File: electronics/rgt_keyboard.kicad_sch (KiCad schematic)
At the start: 30 parts, among them SW30 SW_SPST, SW31 SW_SPST, SW32 SW_SPST, SW33 SW_SPST, SW34 SW_SPST, SW35 SW_SPST, SW36 SW_SPST, SW37 SW_SPST, SW38 SW_SPST, SW39 SW_SPST, SW40 SW_SPST, SW41 SW_SPST, SW42 SW_SPST, SW43 SW_SPST, SW44 SW_SPST, SW45 SW_SPST, SW46 SW_SPST, SW47 SW_SPST, SW48 SW_SPST, SW49 SW_SPST, SW50 SW_SPST, SW51 SW_SPST, SW52 SW_SPST, SW53 SW_SPST, SW54 SW_SPST, SW55 SW_SPST, SW56 SW_SPST, SW57 SW_SPST, SW58 SW_SPST, U3 PCA9506DGG

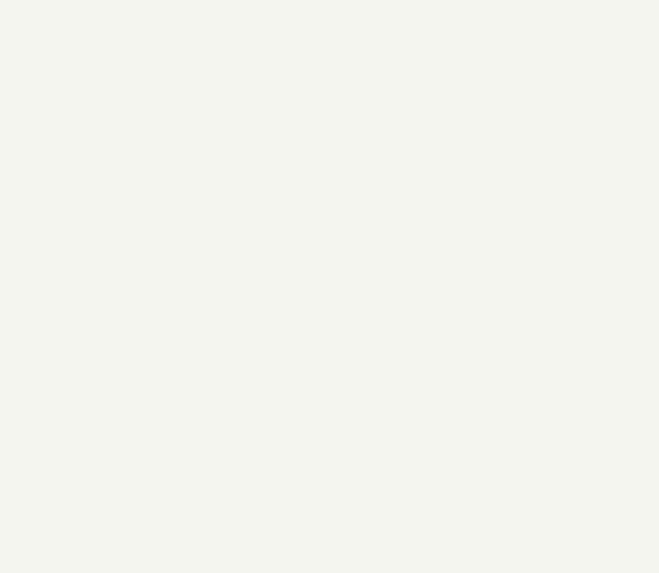
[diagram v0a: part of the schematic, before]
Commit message: add i2c headers to schematic
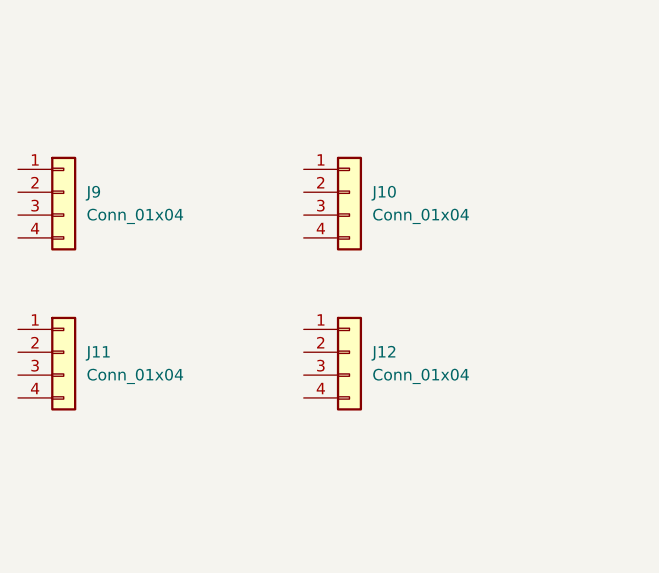
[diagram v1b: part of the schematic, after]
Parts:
- added J10, J11, J12, J9: Conn_01x04, symbol Connector_Generic:Conn_01x04
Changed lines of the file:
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@@
     (pin "2")
+  )
+  (symbol (lib_id "Connector_Generic:Conn_01x04") (at 43.18 66.04 0) (unit 1)
+    (in_bom yes) (on_board yes) (fields_autoplaced)
+    (property "Reference" "J11" (id 0) (at 45.72 66.0399 0)
+      (effects (font (size 1.27 1.27)) (justify left))
+    )
+    (property "Value" "Conn_01x04" (id 1) (at 45.72 68.5799 0)
+      (effects (font (size 1.27 1.27)) (justify left))
+    )
+    (property "Footprint" "" (id 2) (at 43.18 66.04 0)
+      (effects (font (size 1.27 1.27)) hide)
+    )
+    (property "Datasheet" "~" (id 3) (at 43.18 66.04 0)
+      (effects (font (size 1.27 1.27)) hide)
+    )
+    (pin "1")
+    (pin "2")
+    (pin "3")
+    (pin "4")
   )
   (symbol (lib_name "SW_SPST_2") (lib_id "Kailh:SW_SPST") (at 44.45 133.35 0) (unit 1)
@@
     (pin "2")
   )
+  (symbol (lib_id "Connector_Generic:Conn_01x04") (at 43.18 48.26 0) (unit 1)
+    (in_bom yes) (on_board yes) (fields_autoplaced)
+    (property "Reference" "J9" (id 0) (at 45.72 48.2599 0)
+      (effects (font (size 1.27 1.27)) (justify left))
+    )
+    (property "Value" "Conn_01x04" (id 1) (at 45.72 50.7999 0)
+      (effects (font (size 1.27 1.27)) (justify left))
+    )
+    (property "Footprint" "" (id 2) (at 43.18 48.26 0)
+      (effects (font (size 1.27 1.27)) hide)
+    )
+    (property "Datasheet" "~" (id 3) (at 43.18 48.26 0)
+      (effects (font (size 1.27 1.27)) hide)
+    )
+    (pin "1")
+    (pin "2")
+    (pin "3")
+    (pin "4")
+  )
   (symbol (lib_name "SW_SPST_26") (lib_id "Kailh:SW_SPST") (at 44.45 101.6 0) (unit 1)
     (in_bom yes) (on_board yes) (fields_autoplaced)
@@
     (pin "2")
   )
+  (symbol (lib_id "Connector_Generic:Conn_01x04") (at 74.93 66.04 0) (unit 1)
+    (in_bom yes) (on_board yes) (fields_autoplaced)
+    (property "Reference" "J12" (id 0) (at 77.47 66.0399 0)
+      (effects (font (size 1.27 1.27)) (justify left))
+    )
+    (property "Value" "Conn_01x04" (id 1) (at 77.47 68.5799 0)
+      (effects (font (size 1.27 1.27)) (justify left))
+    )
+    (property "Footprint" "" (id 2) (at 74.93 66.04 0)
+      (effects (font (size 1.27 1.27)) hide)
+    )
+    (property "Datasheet" "~" (id 3) (at 74.93 66.04 0)
+      (effects (font (size 1.27 1.27)) hide)
+    )
+    (pin "1")
+    (pin "2")
+    (pin "3")
+    (pin "4")
+  )
+  (symbol (lib_id "Connector_Generic:Conn_01x04") (at 74.93 48.26 0) (unit 1)
+    (in_bom yes) (on_board yes) (fields_autoplaced)
+    (property "Reference" "J10" (id 0) (at 77.47 48.2599 0)
+      (effects (font (size 1.27 1.27)) (justify left))
+    )
+    (property "Value" "Conn_01x04" (id 1) (at 77.47 50.7999 0)
+      (effects (font (size 1.27 1.27)) (justify left))
+    )
+    (property "Footprint" "" (id 2) (at 74.93 48.26 0)
+      (effects (font (size 1.27 1.27)) hide)
+    )
+    (property "Datasheet" "~" (id 3) (at 74.93 48.26 0)
+      (effects (font (size 1.27 1.27)) hide)
+    )
+    (pin "1")
+    (pin "2")
+    (pin "3")
+    (pin "4")
+  )
   (symbol (lib_name "SW_SPST_4") (lib_id "Kailh:SW_SPST") (at 64.77 149.86 0) (unit 1)

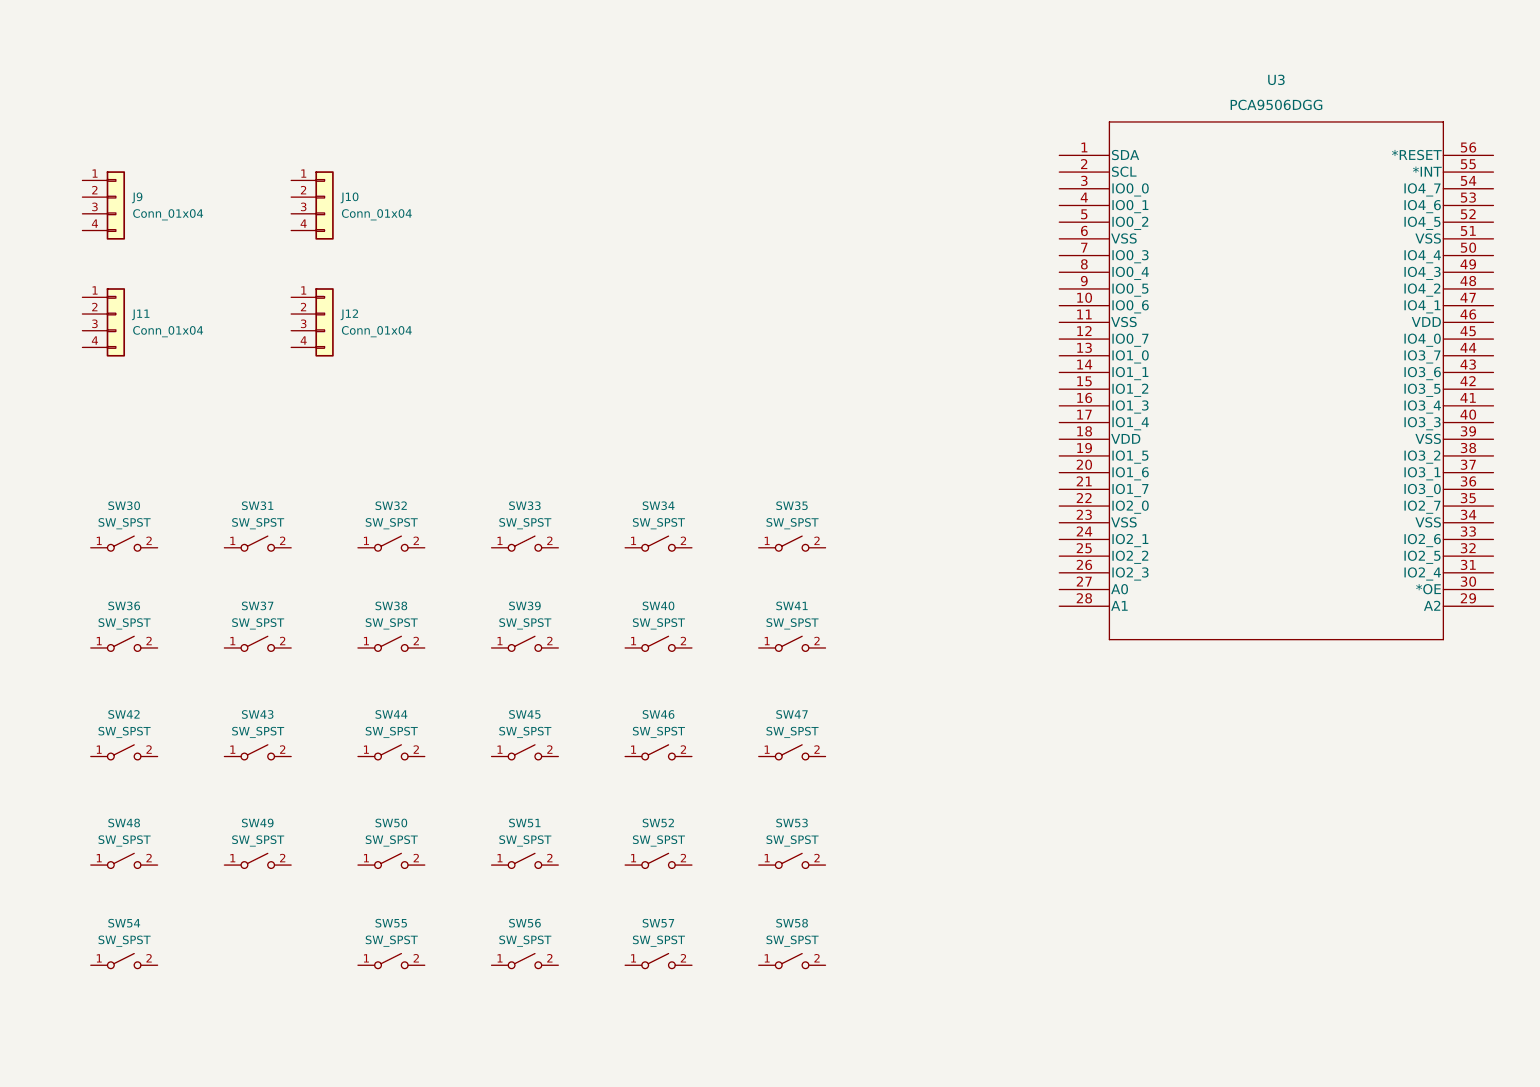
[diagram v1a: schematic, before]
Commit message: label switch nets
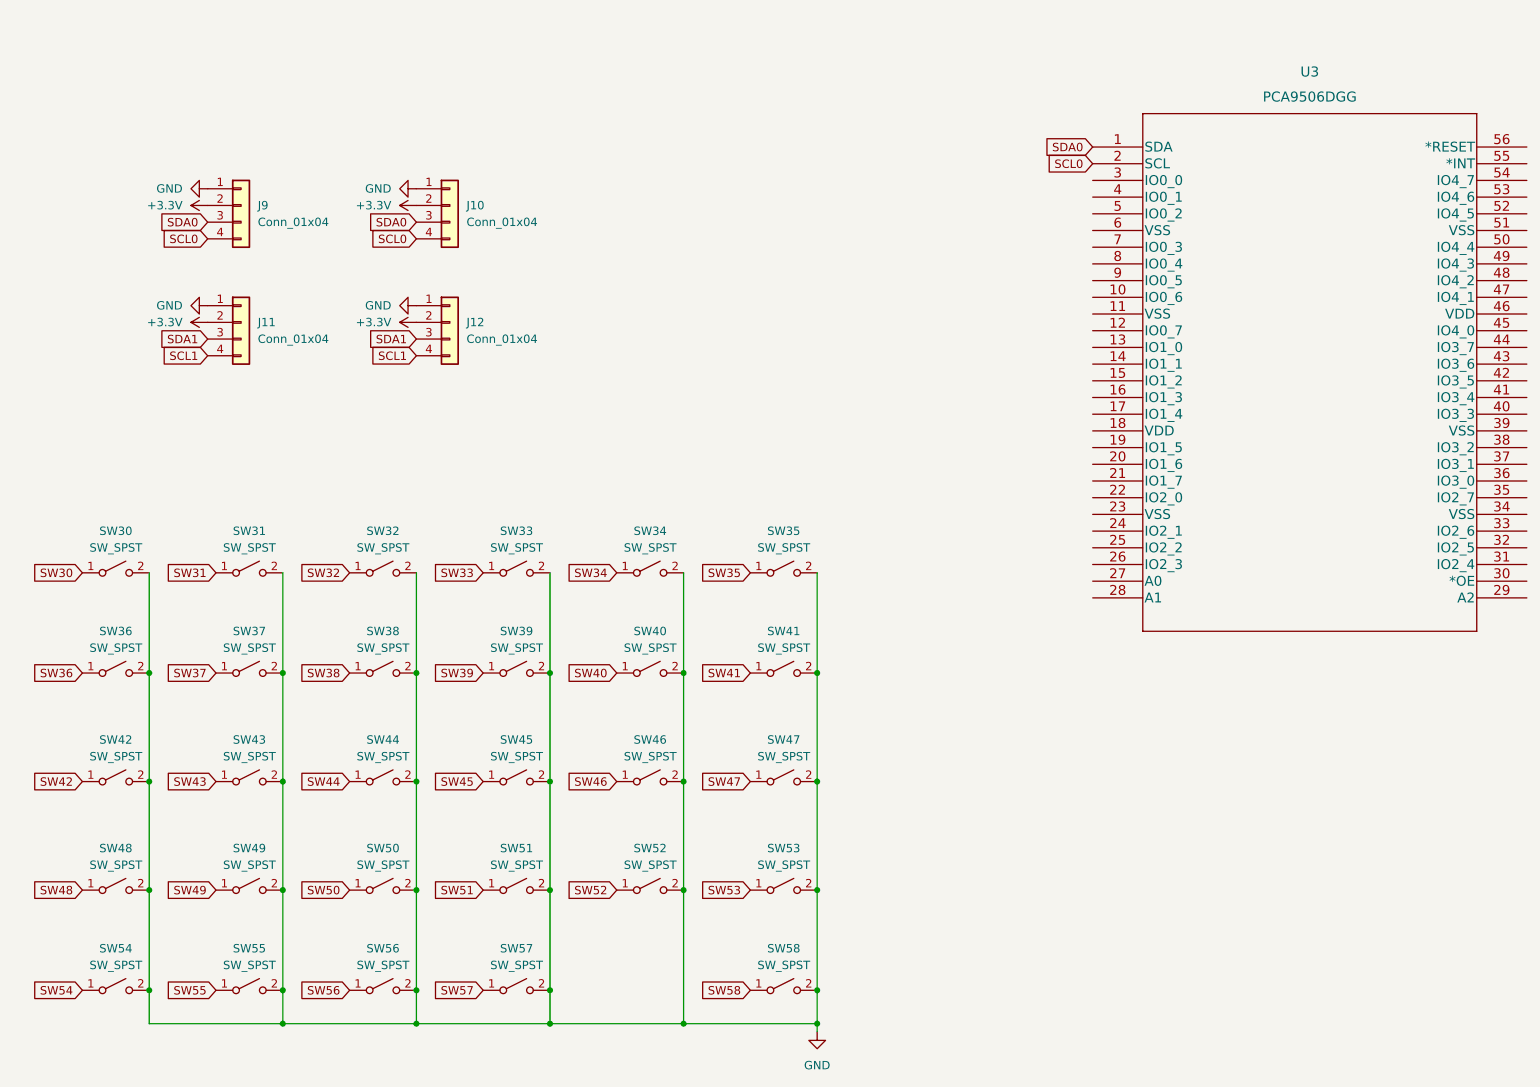
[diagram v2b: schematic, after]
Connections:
- net SW31: now reaches SW31.1 (A)
- net GND: now reaches SW31.2 (B)
- net GND: now also J10.1 (Pin_1), J11.1 (Pin_1), J12.1 (Pin_1), J9.1 (Pin_1), SW30.2 (B), SW32.2 (B), SW33.2 (B), SW34.2 (B), SW35.2 (B), SW36.2 (B), SW37.2 (B), SW38.2 (B), SW39.2 (B), SW40.2 (B), SW41.2 (B), SW42.2 (B), SW43.2 (B), SW44.2 (B), SW45.2 (B), SW46.2 (B), SW47.2 (B), SW48.2 (B), SW49.2 (B), SW50.2 (B), SW51.2 (B), SW52.2 (B), SW53.2 (B), SW54.2 (B), SW55.2 (B), SW56.2 (B), SW57.2 (B), SW58.2 (B)
- net SW44: now reaches SW44.1 (A)
- net SW39: now reaches SW39.1 (A)
- net +3V3: now reaches J11.2 (Pin_2)
- net +3V3: now also J10.2 (Pin_2), J12.2 (Pin_2), J9.2 (Pin_2)
- net SDA1: now reaches J11.3 (Pin_3)
- net SDA1: now also J12.3 (Pin_3)
- net SCL1: now reaches J11.4 (Pin_4)
- net SCL1: now also J12.4 (Pin_4)
- net SW42: now reaches SW42.1 (A)
- net SW55: now reaches SW55.1 (A)
- net SDA0: now reaches J9.3 (Pin_3)
- net SDA0: now also J10.3 (Pin_3), U3.1 (SDA)
- net SCL0: now reaches J9.4 (Pin_4)
- net SCL0: now also J10.4 (Pin_4), U3.2 (SCL)
- net SW30: now reaches SW30.1 (A)
- net SW37: now reaches SW37.1 (A)
- net SW49: now reaches SW49.1 (A)
- net SW46: now reaches SW46.1 (A)
- net SW50: now reaches SW50.1 (A)
- net SW40: now reaches SW40.1 (A)
- net SW32: now reaches SW32.1 (A)
- net SW45: now reaches SW45.1 (A)
- net SW52: now reaches SW52.1 (A)
- net SW33: now reaches SW33.1 (A)
- net SW35: now reaches SW35.1 (A)
- net SW36: now reaches SW36.1 (A)
- net SW34: now reaches SW34.1 (A)
- net SW54: now reaches SW54.1 (A)
- net SW57: now reaches SW57.1 (A)
- net SW53: now reaches SW53.1 (A)
- net SW41: now reaches SW41.1 (A)
- net SW38: now reaches SW38.1 (A)
- net SW48: now reaches SW48.1 (A)
- net SW51: now reaches SW51.1 (A)
- net SW43: now reaches SW43.1 (A)
- net SW47: now reaches SW47.1 (A)
- net SW56: now reaches SW56.1 (A)
- net SW58: now reaches SW58.1 (A)

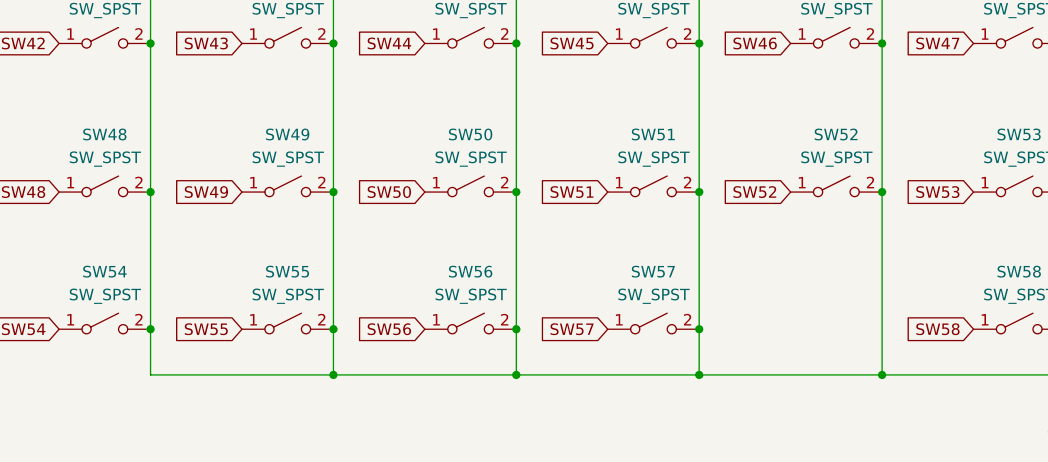
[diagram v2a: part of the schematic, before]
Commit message: move some switches
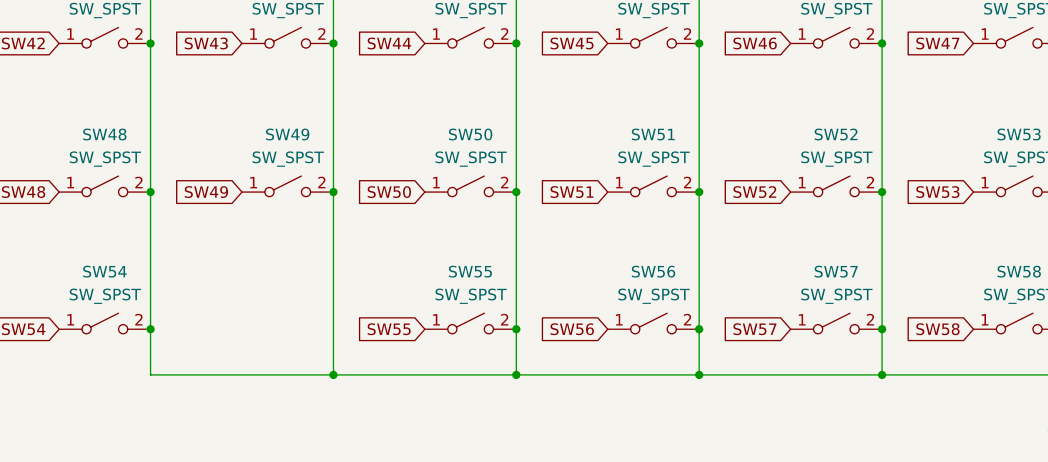
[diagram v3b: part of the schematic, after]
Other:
- moved on the sheet: SW55, SW56, SW57

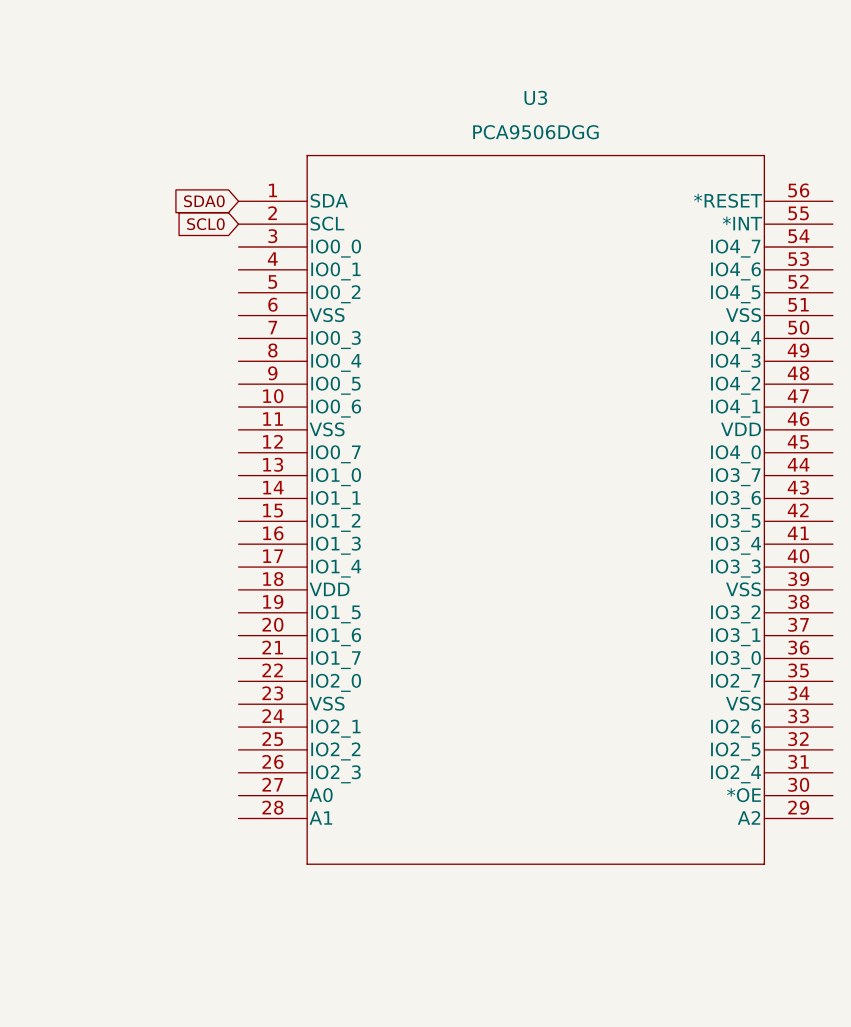
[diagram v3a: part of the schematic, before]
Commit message: change IO expander
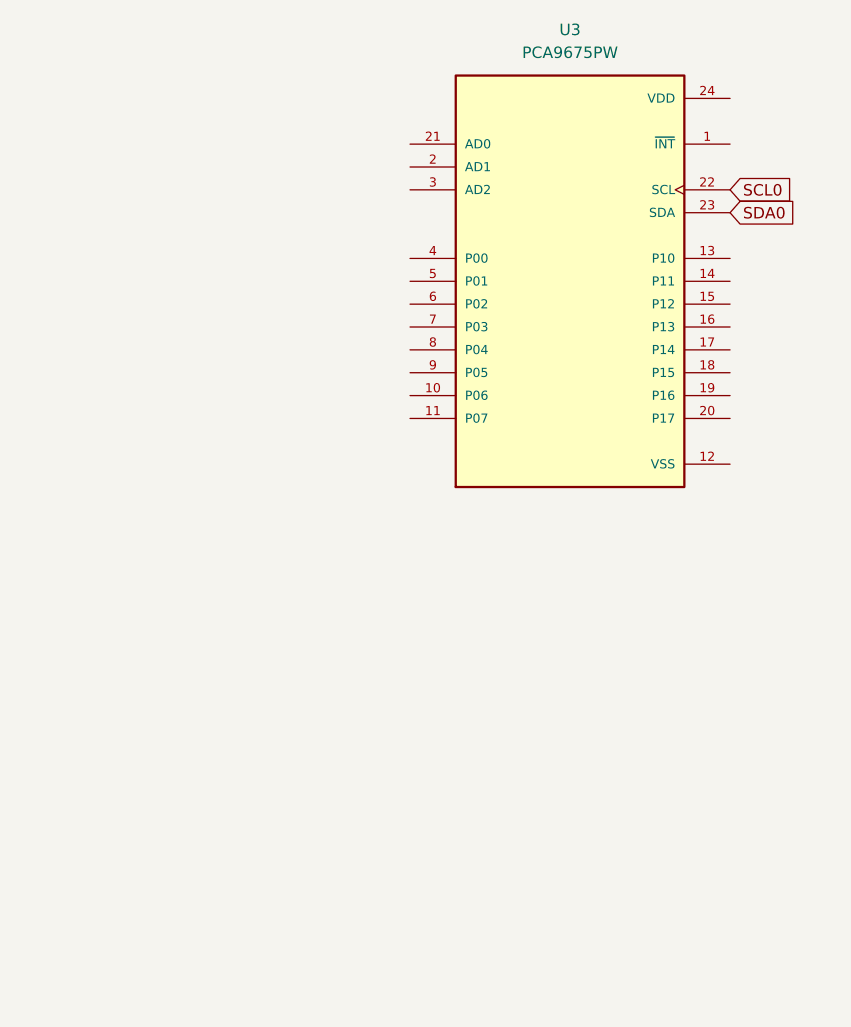
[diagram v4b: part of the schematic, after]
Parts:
- removed U3: PCA9506DGG, PCA9506:PCA9506DGG, symbol PCA9506:PCA9506DGG
- added U3: PCA9675PW, PCA9675PW:SOP65P640X110-24N, symbol PCA9675PW_118:PCA9675PW
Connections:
- net SCL0: now also U3.22 (SCL)
- net SDA0: now also U3.23 (SDA)
